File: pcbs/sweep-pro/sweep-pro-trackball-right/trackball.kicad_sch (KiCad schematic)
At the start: 11 parts, among them U6 PMW3610, U7 MCP1700-1802E-TT

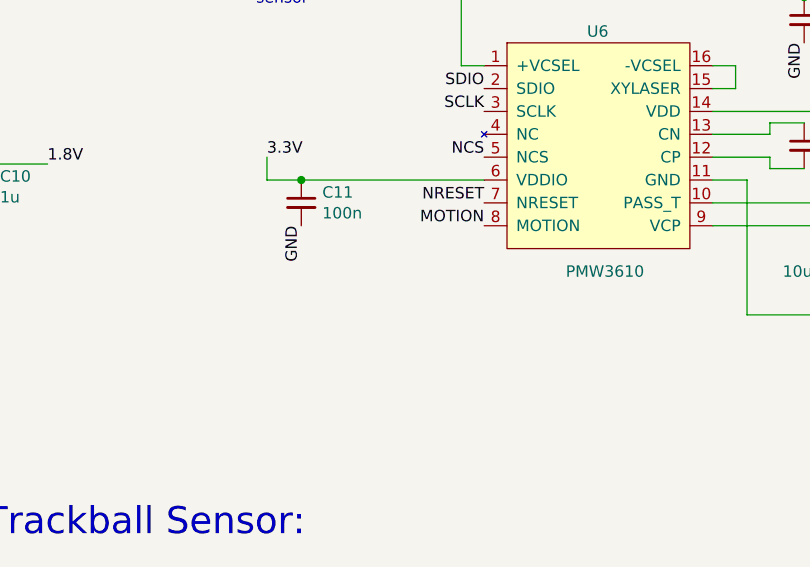
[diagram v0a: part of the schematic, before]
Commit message: init version with integrated trackball in thumb position
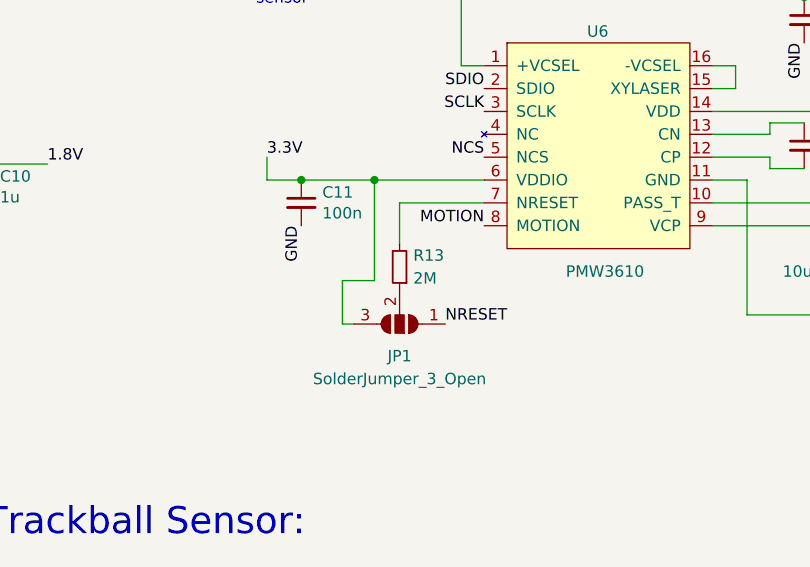
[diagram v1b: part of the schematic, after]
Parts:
- added JP1: SolderJumper_3_Open, Jumper:SolderJumper-3_P1.3mm_Open_RoundedPad1.0x1.5mm_NumberLabels, symbol Jumper:SolderJumper_3_Open
- added R13: 2M, Resistor_SMD:R_0603_1608Metric, symbol Device:R_Small
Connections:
- net 3.3V: now also JP1.3 (B)
- net NRESET: now also JP1.1 (A); no longer U6.7 (NRESET)
- new net: JP1.2 (C), R13.1
- new net: R13.2, U6.7 (NRESET)
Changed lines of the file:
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@@
 (kicad_sch (version 20211123) (generator eeschema)
   (paper "A4")
+  (junction (at 130.81 74.422) (diameter 0) (color 0 0 0 0)
+  )
   (junction (at 178.562 54.102) (diameter 0) (color 0 0 0 0)
   )
@@
     (stroke (width 0) (type default) (color 0 0 0 0))
   )
+  (wire (pts (xy 133.604 76.962) (xy 133.604 81.534))
+    (stroke (width 0) (type default) (color 0 0 0 0))
+  )
   (wire (pts (xy 64.008 77.724) (xy 64.008 84.074))
     (stroke (width 0) (type default) (color 0 0 0 0))
@@
     (stroke (width 0) (type default) (color 0 0 0 0))
   )
+  (wire (pts (xy 127.254 90.424) (xy 128.524 90.424))
+    (stroke (width 0) (type default) (color 0 0 0 0))
+  )
   (wire (pts (xy 178.562 54.102) (xy 140.462 54.102))
     (stroke (width 0) (type default) (color 0 0 0 0))
@@
     (stroke (width 0) (type default) (color 0 0 0 0))
   )
+  (wire (pts (xy 130.81 85.598) (xy 127.254 85.598))
+    (stroke (width 0) (type default) (color 0 0 0 0))
+  )
   (wire (pts (xy 188.722 62.992) (xy 195.072 62.992))
     (stroke (width 0) (type default) (color 0 0 0 0))
@@
     (stroke (width 0) (type default) (color 0 0 0 0))
   )
+  (wire (pts (xy 130.81 74.422) (xy 130.81 85.598))
+    (stroke (width 0) (type default) (color 0 0 0 0))
+  )
   (polyline (pts (xy 150.876 90.932) (xy 150.876 90.932))
     (stroke (width 0) (type default) (color 0 0 0 0))
@@
     (stroke (width 0) (type default) (color 0 0 0 0))
   )
-  (wire (pts (xy 122.682 74.422) (xy 143.002 74.422))
+  (wire (pts (xy 122.682 74.422) (xy 130.81 74.422))
     (stroke (width 0) (type default) (color 0 0 0 0))
   )
@@
     (stroke (width 0) (type default) (color 0 0 0 0))
   )
+  (wire (pts (xy 127.254 85.598) (xy 127.254 90.424))
+    (stroke (width 0) (type default) (color 0 0 0 0))
+  )
   (wire (pts (xy 186.182 79.502) (xy 193.802 79.502))
     (stroke (width 0) (type default) (color 0 0 0 0))
@@
     (stroke (width 0) (type default) (color 0 0 0 0))
   )
+  (wire (pts (xy 133.604 76.962) (xy 143.002 76.962))
+    (stroke (width 0) (type default) (color 0 0 0 0))
+  )
   (wire (pts (xy 182.88 89.408) (xy 189.992 89.408))
     (stroke (width 0) (type default) (color 0 0 0 0))
   )
   (wire (pts (xy 24.892 31.496) (xy 34.29 31.496))
+    (stroke (width 0) (type default) (color 0 0 0 0))
+  )
+  (wire (pts (xy 130.81 74.422) (xy 143.002 74.422))
     (stroke (width 0) (type default) (color 0 0 0 0))
   )
@@
     (effects (font (size 1.27 1.27)) (justify left bottom))
   )
+  (label "NRESET" (at 138.684 90.424 0)
+    (effects (font (size 1.27 1.27)) (justify left bottom))
+  )
   (label "SDIO" (at 143.002 64.262 180)
     (effects (font (size 1.27 1.27)) (justify right bottom))
@@
   )
   (label "GND" (at 178.562 59.182 270)
-    (effects (font (size 1.27 1.27)) (justify right bottom))
-  )
-  (label "NRESET" (at 143.002 76.962 180)
     (effects (font (size 1.27 1.27)) (justify right bottom))
   )
@@
     )
     (property "LCSC" "C14663" (id 4) (at 64.008 75.184 0)
+      (effects (font (size 1.27 1.27)) hide)
+    )
+    (pin "1")
+    (pin "2")
+  )
+  (symbol (lib_id "Device:R_Small") (at 133.604 84.074 180) (unit 1)
+    (in_bom yes) (on_board yes) (fields_autoplaced)
+    (property "Reference" "R13" (id 0) (at 135.128 82.8039 0)
+      (effects (font (size 1.27 1.27)) (justify right))
+    )
+    (property "Value" "2M" (id 1) (at 135.128 85.3439 0)
+      (effects (font (size 1.27 1.27)) (justify right))
+    )
+    (property "Footprint" "Resistor_SMD:R_0603_1608Metric" (id 2) (at 133.604 84.074 0)
+      (effects (font (size 1.27 1.27)) hide)
+    )
+    (property "Datasheet" "~" (id 3) (at 133.604 84.074 0)
       (effects (font (size 1.27 1.27)) hide)
     )
@@
       (effects (font (size 1.27 1.27)) hide)
     )
+    (pin "1")
+    (pin "2")
+    (pin "3")
+  )
+  (symbol (lib_id "Jumper:SolderJumper_3_Open") (at 133.604 90.424 180) (unit 1)
+    (in_bom yes) (on_board yes) (fields_autoplaced)
+    (property "Reference" "JP1" (id 0) (at 133.604 93.98 0))
+    (property "Value" "SolderJumper_3_Open" (id 1) (at 133.604 96.52 0))
+    (property "Footprint" "Jumper:SolderJumper-3_P1.3mm_Open_RoundedPad1.0x1.5mm_NumberLabels" (id 2) (at 133.604 90.424 0)
+      (effects (font (size 1.27 1.27)) hide)
+    )
+    (property "Datasheet" "~" (id 3) (at 133.604 90.424 0)
+      (effects (font (size 1.27 1.27)) hide)
+    )
